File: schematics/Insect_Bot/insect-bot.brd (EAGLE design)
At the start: 40.3 x 78.7 mm, 26 parts, among them Q1 2N2222, U1 L4931-TO92-AMMO, U2 ARDUINO_MINI

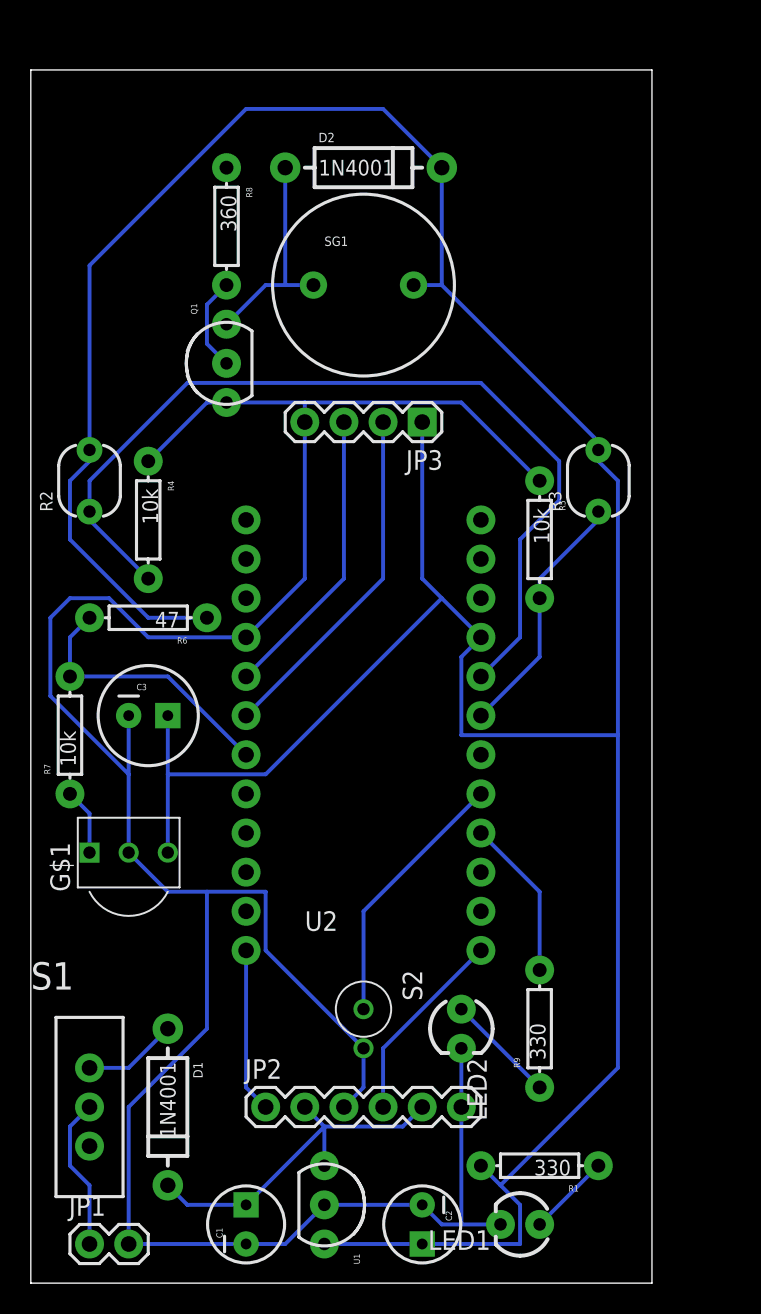
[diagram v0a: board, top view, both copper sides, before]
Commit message: First completed insect bot PCB.
First revision with poured-copper ground plane.
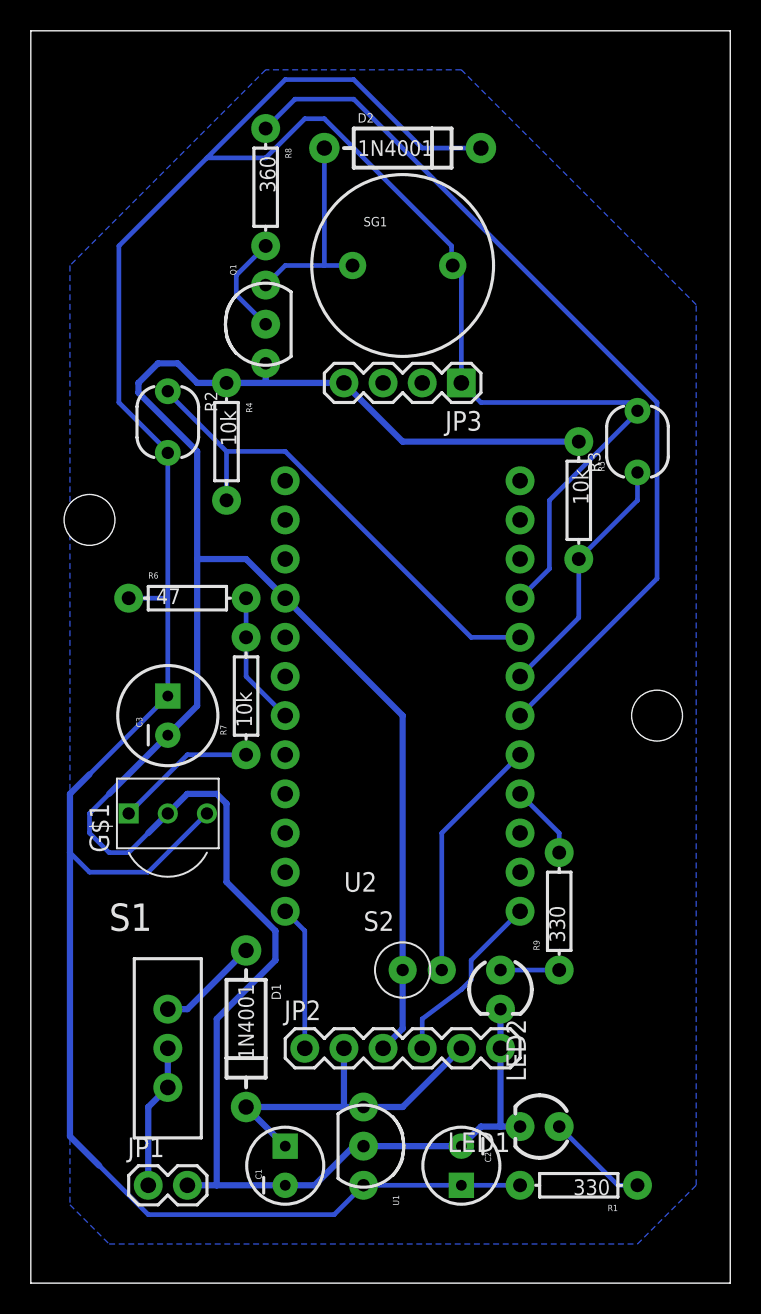
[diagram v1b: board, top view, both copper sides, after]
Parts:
- added JP4, JP5: STAND-OFF, SparkFun-Electromechanical:STAND-OFF
- S2: value TILTSWITCH -> tilt
- moved R7 11.7 mm to (14.0, 38.1)
- moved R9 7.73 mm to (34.3, 24.1)
- moved D1 7.18 mm to (14.0, 16.5)
- moved R4 7.18 mm to (12.7, 54.6)
- moved LED1 6.48 mm to (33.0, 10.2)
- moved R2 6.35 mm to (8.89, 55.9), turned to 270 degrees
- moved S1 6.35 mm to (8.89, 15.2)
- moved JP1 5.39 mm to (7.62, 6.35)
- moved C2 4.58 mm to (27.9, 7.62)
- moved JP2 4.58 mm to (17.8, 15.2)
- moved C1 4.58 mm to (16.5, 7.62)
- moved U1 4.58 mm to (21.6, 8.89)
- moved R8 3.59 mm to (15.2, 71.1)
- moved JP3 3.59 mm to (27.9, 58.4)
- moved IRM1 3.59 mm to (8.89, 30.5)
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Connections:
- net GND: now also S2.1; no longer S2.2
- net N$1: now also S1.3
- net N$12: now also S2.2; no longer S2.1
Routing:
- net N$6: track 0.00 -> 58.3 mm
- net N$8: track 59.2 -> 32.7 mm
- net TRIGGER: track 22.7 -> 0.00 mm
- net VCC: track 216.5 -> 194.9 mm
- net ECHO: track 19.1 -> 0.00 mm
- net N$9: track 17.9 -> 8.67 mm
- net N$13: track 10.5 -> 4.86 mm
- net GND: track 170.5 -> 175.5 mm
- net REMOTE: track 4.34 -> 9.20 mm
- net N$14: track 7.18 -> 3.81 mm
- net N$4: track 10.7 -> 9.42 mm
- net N$3: track 5.39 -> 6.66 mm
- net N$5: track 12.8 -> 11.7 mm
- net N$12: track 17.1 -> 16.1 mm
- net V_IN: track 24.0 -> 23.0 mm
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- added copper zone on layer 16, net GND
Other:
- board size 40.3 x 78.7 mm -> 45.4 x 81.3 mm
